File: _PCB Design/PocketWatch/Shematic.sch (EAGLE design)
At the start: 1 part

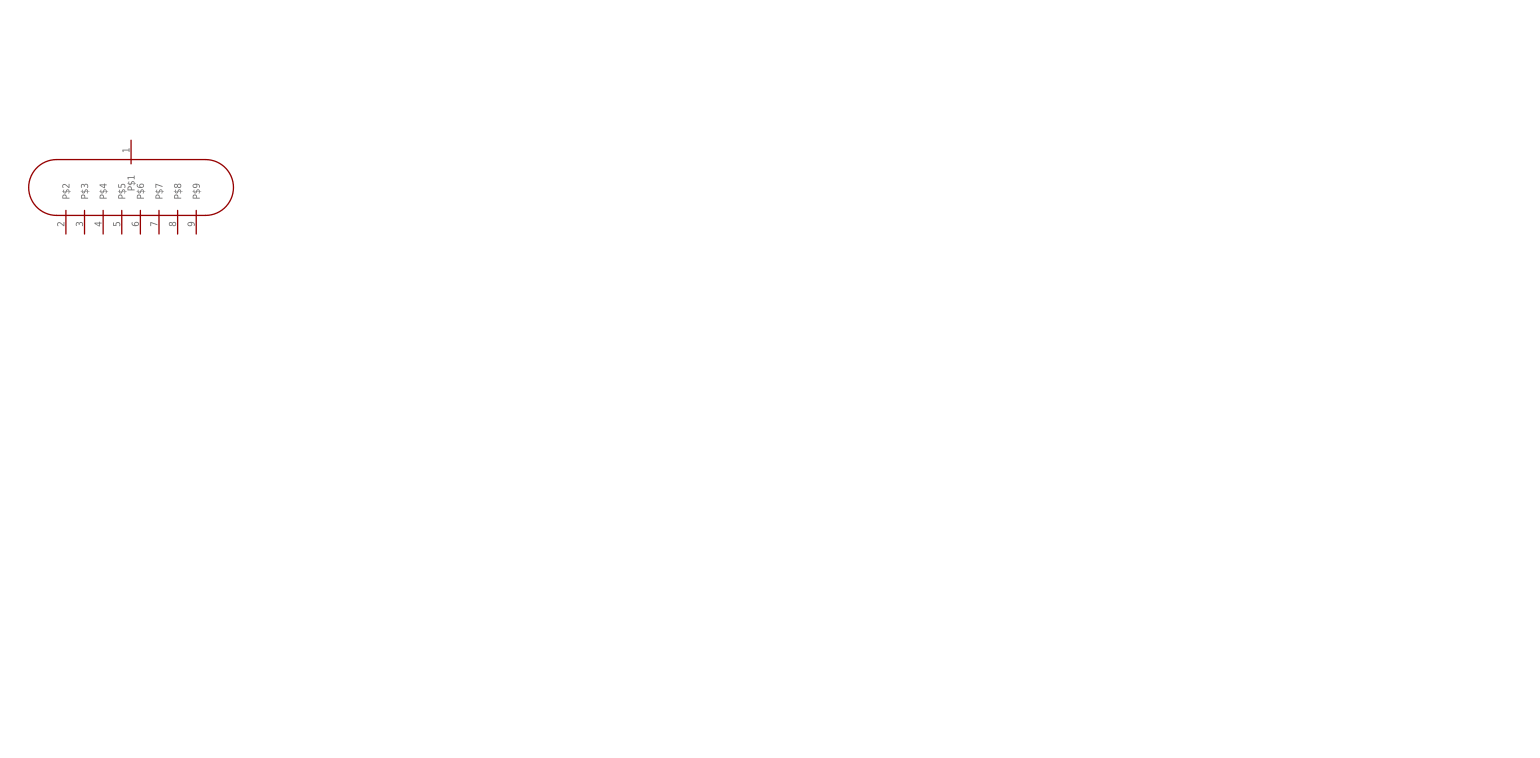
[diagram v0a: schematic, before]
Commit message: Connected IV-9 tubes to microcontroller
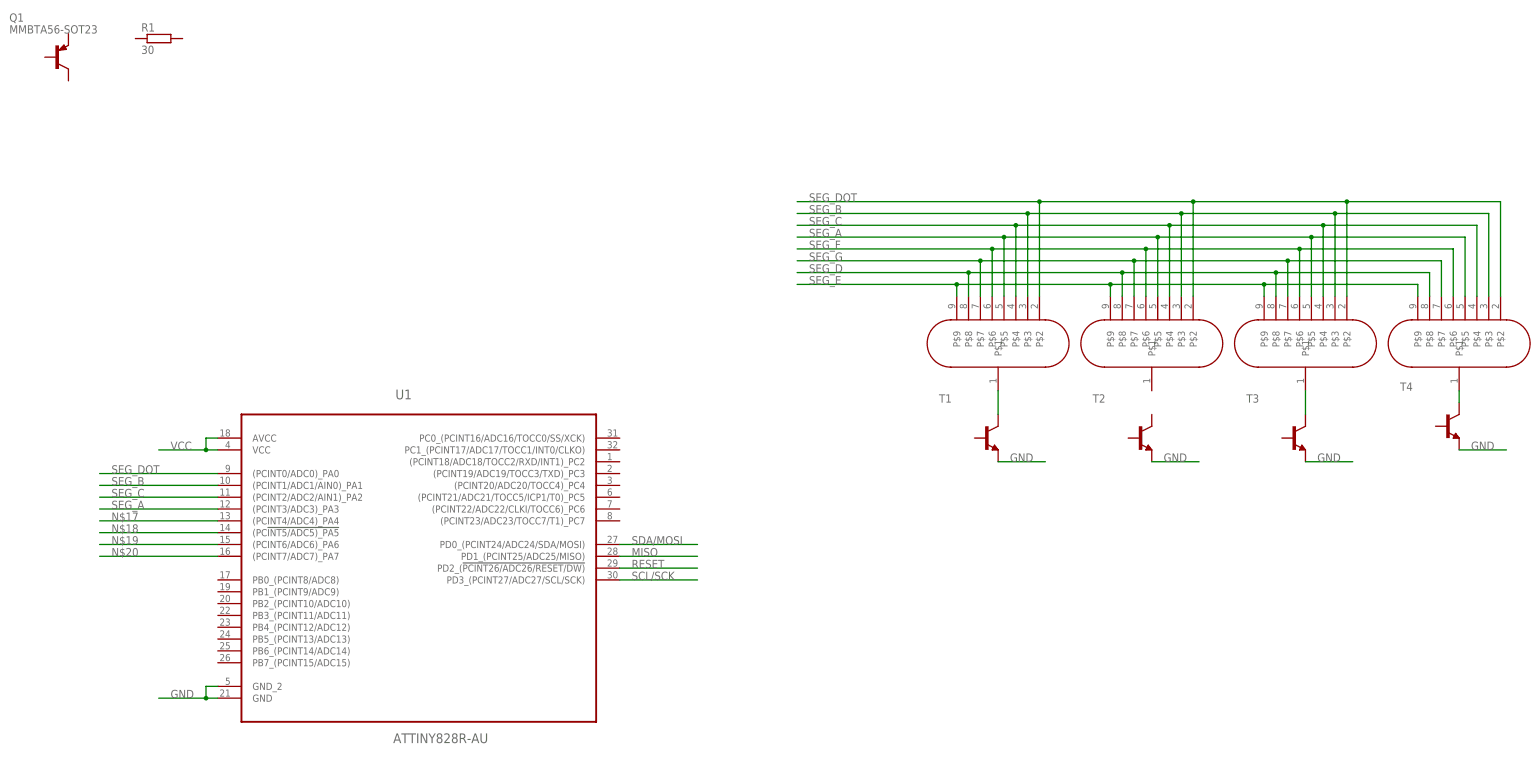
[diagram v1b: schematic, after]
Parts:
- added Q1: MMBTA56-SOT23, transistor-pnp:MMBTA56-SOT23
- added R1: 30, eagle-ltspice:RR1206
- added T1, T2, T3, T4: (no value), transistor:MMBT918LT1-NPN-SOT23-BEC
- added U$2, U$3, U$4: IV-9, Library:IV-9
- added U1: ATTINY828R-AU, Library:ATTINY828R-AU
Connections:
- new net GND: T1.E, T2.E, T3.E, T4.E, U1.GND, U1.GND_2
- new net MISO: U1.PD1_(PCINT25/ADC25/MISO)
- new net N$17: U1.(PCINT4/ADC4)_PA4
- new net N$18: U1.(PC!INT5/ADC5)_PA5
- new net N$19: U1.(PCINT6/ADC6)_PA6
- new net N$2: T3.C, U$2.P$1
- new net N$20: U1.(PCINT7/ADC7)_PA7
- new net N$3: T4.C, U$1.P$1
- new net N$5: T1.C, U$3.P$1
- new net RESET: U1.PD2_(!PCINT26/ADC26/RESET/DW)
- new net SCL/SCK: U1.PD3_(PCINT27/ADC27/SCL/SCK)
- new net SDA/MOSI: U1.PD0_(PCINT24/ADC24/SDA/MOSI)
- new net SEG_A: U$1.P$5, U$2.P$5, U$3.P$5, U$4.P$5, U1.(PCINT3/ADC3)_PA3
- new net SEG_B: U$1.P$3, U$2.P$3, U$3.P$3, U$4.P$3, U1.(PCINT1/ADC1/AIN0)_PA1
- new net SEG_C: U$1.P$4, U$2.P$4, U$3.P$4, U$4.P$4, U1.(PCINT2/ADC2/AIN1)_PA2
- new net SEG_D: U$1.P$8, U$2.P$8, U$3.P$8, U$4.P$8
- new net SEG_DOT: U$1.P$2, U$2.P$2, U$3.P$2, U$4.P$2, U1.(PCINT0/ADC0)_PA0
- new net SEG_E: U$1.P$9, U$2.P$9, U$3.P$9, U$4.P$9
- new net SEG_F: U$1.P$6, U$2.P$6, U$3.P$6, U$4.P$6
- new net SEG_G: U$1.P$7, U$2.P$7, U$3.P$7, U$4.P$7
- new net VCC: U1.AVCC, U1.VCC

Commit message: Switched design to use ATTINY88 instead of ATTINY828R to gain master I2C functionality.
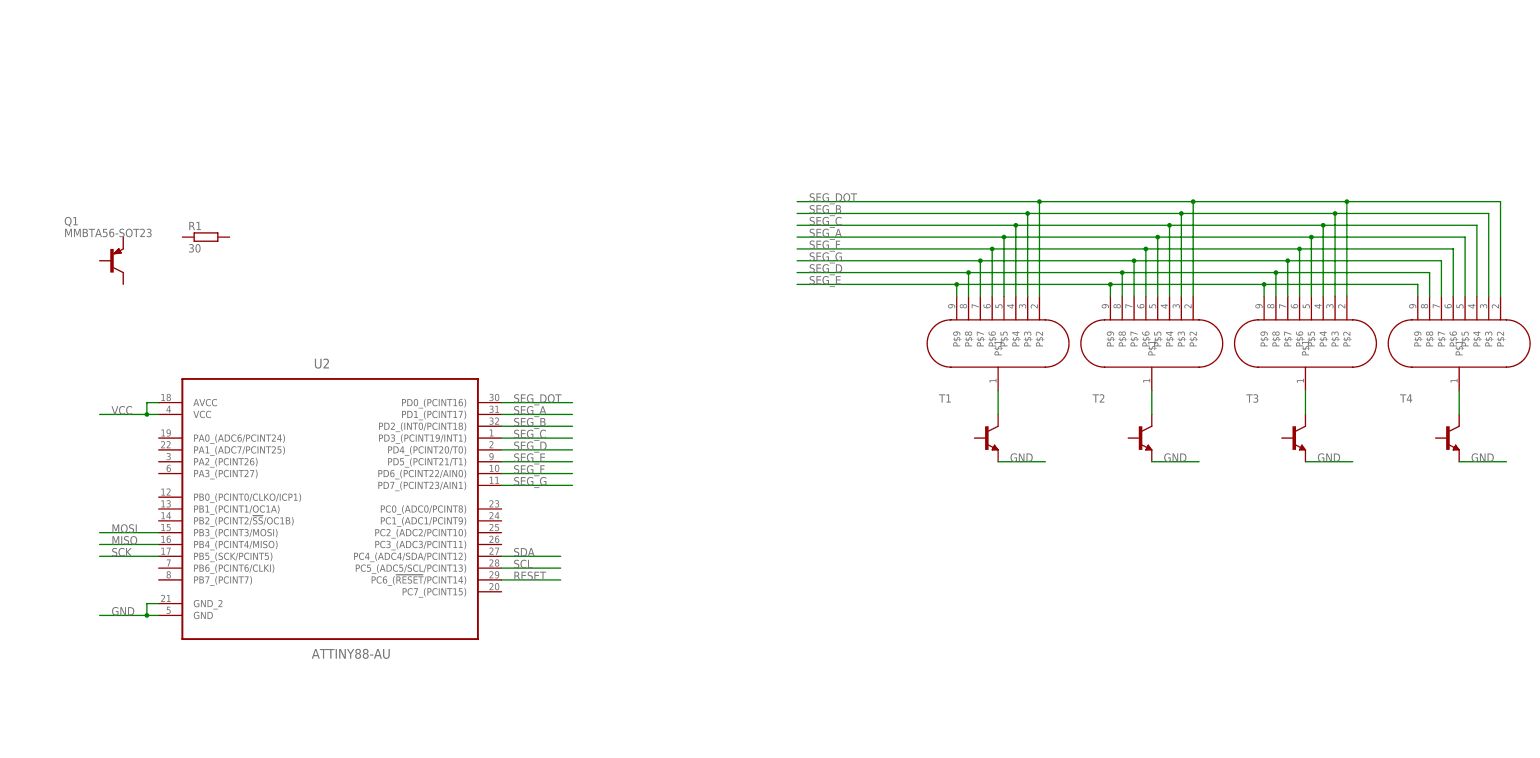
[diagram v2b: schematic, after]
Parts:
- removed U1: ATTINY828R-AU, Library:ATTINY828R-AU
- added U2: ATTINY88-AU, Library:ATTINY88-AU
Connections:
- removed net N$17: U1.(PCINT4/ADC4)_PA4
- removed net N$18: U1.(PC!INT5/ADC5)_PA5
- removed net N$19: U1.(PCINT6/ADC6)_PA6
- removed net N$20: U1.(PCINT7/ADC7)_PA7
- removed net SCL/SCK: U1.PD3_(PCINT27/ADC27/SCL/SCK)
- removed net SDA/MOSI: U1.PD0_(PCINT24/ADC24/SDA/MOSI)
- new net MOSI: U2.PB3_(PCINT3/MOSI)
- new net N$1: T2.C, U$4.P$1
- new net SCK: U2.PB5_(SCK/PCINT5)
- new net SCL: U2.PC5_(ADC5/SCL/PCINT13)
- new net SDA: U2.PC4_(ADC4/SDA/PCINT12)
- net GND: now also U2.GND, U2.GND_2; no longer U1.GND, U1.GND_2
- net MISO: now also U2.PB4_(PCINT4/MISO); no longer U1.PD1_(PCINT25/ADC25/MISO)
- net RESET: now also U2.PC6_(!RESET!/PCINT14); no longer U1.PD2_(!PCINT26/ADC26/RESET/DW)
- net SEG_A: now also U2.PD1_(PCINT17); no longer U1.(PCINT3/ADC3)_PA3
- net SEG_B: now also U2.PD2_(INT0/PCINT18); no longer U1.(PCINT1/ADC1/AIN0)_PA1
- net SEG_C: now also U2.PD3_(PCINT19/INT1); no longer U1.(PCINT2/ADC2/AIN1)_PA2
- net SEG_D: now also U2.PD4_(PCINT20/T0)
- net SEG_DOT: now also U2.PD0_(PCINT16); no longer U1.(PCINT0/ADC0)_PA0
- net SEG_E: now also U2.PD5_(PCINT21/T1)
- net SEG_F: now also U2.PD6_(PCINT22/AIN0)
- net SEG_G: now also U2.PD7_(PCINT23/AIN1)
- net VCC: now also U2.AVCC, U2.VCC; no longer U1.AVCC, U1.VCC
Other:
- moved on the sheet: Q1, R1, T4

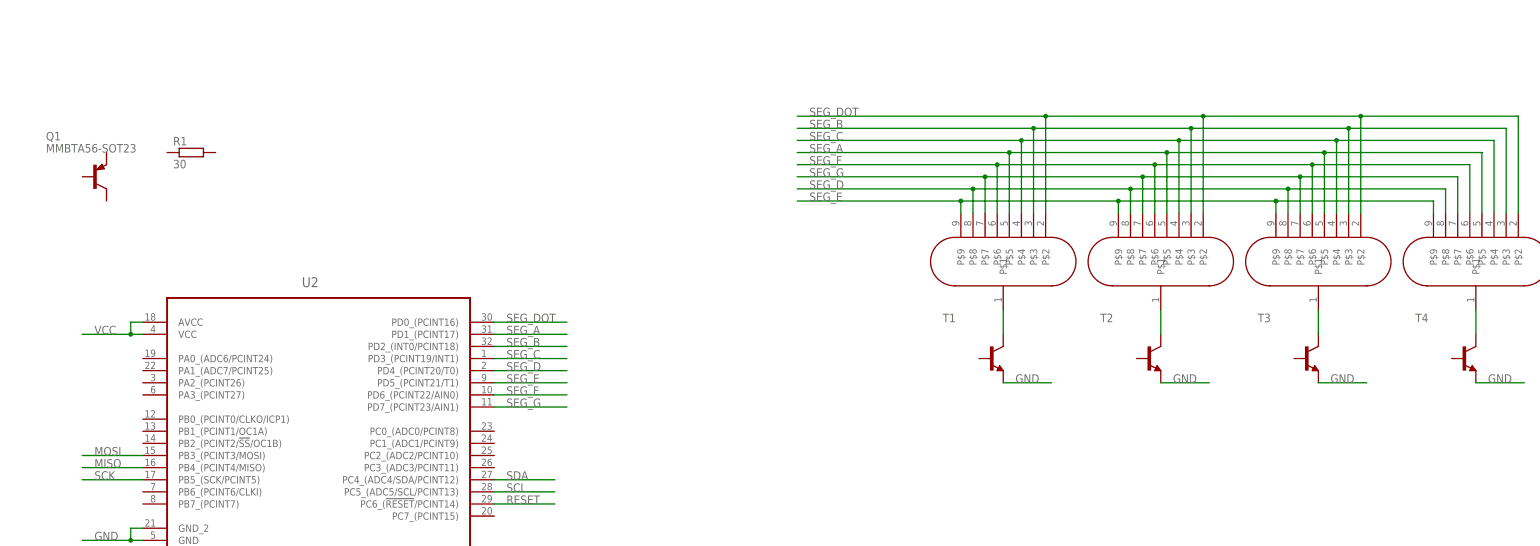
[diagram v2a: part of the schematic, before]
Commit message: Added RTC
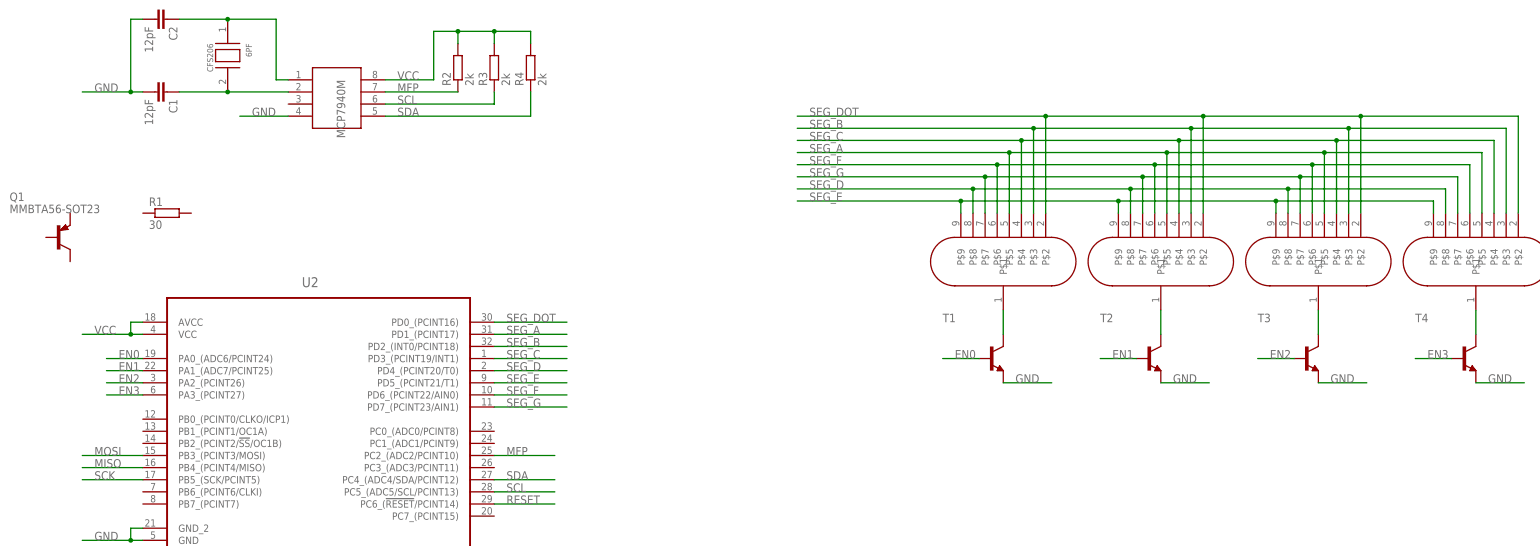
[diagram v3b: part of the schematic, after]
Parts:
- added 6PF: CFS206, Library:CFS206
- added C1, C2: 12pF, eagle-ltspice:CC1206
- added MCP7940M: SOIC-8, smd-footprints:SOIC-8
- added R2, R3, R4: 2k, eagle-ltspice:RR1206
- added U$5: FX135, Library:FX135
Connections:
- new net EN0: T1.B, U2.PA0_(ADC6/PCINT24)
- new net EN1: T2.B, U2.PA1_(ADC7/PCINT25)
- new net EN2: T3.B, U2.PA2_(PCINT26)
- new net EN3: T4.B, U2.PA3_(PCINT27)
- new net MFP: MCP7940M.P$7, R2.1, U2.PC2_(ADC2/PCINT10)
- new net N$4: 6PF.P$2, C1.1, MCP7940M.P$2
- new net N$6: 6PF.P$1, C2.1, MCP7940M.P$1
- net GND: now also C1.2, C2.2, MCP7940M.P$4
- net SCL: now also MCP7940M.P$6, R3.1
- net SDA: now also MCP7940M.P$5, R4.1
- net VCC: now also MCP7940M.P$8, R2.2, R3.2, R4.2
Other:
- moved on the sheet: Q1, R1

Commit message: Added Voltage Regulator, Designed for tubes to be on second board.
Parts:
- removed U$5: FX135, Library:FX135
- added C3: 12pF, eagle-ltspice:CC1206
- added C4, C5: 10uF, eagle-ltspice:CC1206
- added NCP1117: DPAK, smd-footprints:DPAK
- added PAD1: WIREPAD2,54/1,1, wirepad:WIREPAD2,54/1,1
- added SV1, SV2: (no value), con-lstb:MA08-1
- added SV3, SV4, SV5: (no value), con-lstb:MA04-1
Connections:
- removed net N$1: T2.C, U$4.P$1
- removed net N$2: T3.C, U$2.P$1
- removed net N$3: T4.C, U$1.P$1
- removed net N$5: T1.C, U$3.P$1
- new net SEG_A_2: SV2.4, U$1.P$5, U$2.P$5, U$3.P$5, U$4.P$5
- new net SEG_B_2: SV2.2, U$1.P$3, U$2.P$3, U$3.P$3, U$4.P$3
- new net SEG_C_2: SV2.3, U$1.P$4, U$2.P$4, U$3.P$4, U$4.P$4
- new net SEG_DOT_2: SV2.1, U$1.P$2, U$2.P$2, U$3.P$2, U$4.P$2
- new net SEG_D_2: SV2.7, U$1.P$8, U$2.P$8, U$3.P$8, U$4.P$8
- new net SEG_E_2: SV2.8, U$1.P$9, U$2.P$9, U$3.P$9, U$4.P$9
- new net SEG_F_2: SV2.5, U$1.P$6, U$2.P$6, U$3.P$6, U$4.P$6
- new net SEG_G_2: SV2.6, U$1.P$7, U$2.P$7, U$3.P$7, U$4.P$7
- new net TG0: SV5.4, T1.C
- new net TG0_2: SV3.4, U$3.P$1
- new net TG1: SV5.3, T2.C
- new net TG1_2: SV3.3, U$4.P$1
- new net TG2: SV5.2
- new net TG2_2: SV3.2, U$2.P$1
- new net TG3: SV5.1, T3.C
- new net TG3_2: SV3.1, U$1.P$1
- new net TG4: T4.C
- new net VIN: C4.1, NCP1117.P$3
- net EN0: now also SV4.4
- net EN1: now also SV4.3
- net EN2: now also SV4.2
- net EN3: now also SV4.1
- net GND: now also C4.2, C5.2, NCP1117.P$1
- net SEG_A: now also SV1.2; no longer U$1.P$5, U$2.P$5, U$3.P$5, U$4.P$5
- net SEG_B: now also SV1.3; no longer U$1.P$3, U$2.P$3, U$3.P$3, U$4.P$3
- net SEG_C: now also SV1.4; no longer U$1.P$4, U$2.P$4, U$3.P$4, U$4.P$4
- net SEG_D: now also SV1.5; no longer U$1.P$8, U$2.P$8, U$3.P$8, U$4.P$8
- net SEG_DOT: now also SV1.1; no longer U$1.P$2, U$2.P$2, U$3.P$2, U$4.P$2
- net SEG_E: now also SV1.6; no longer U$1.P$9, U$2.P$9, U$3.P$9, U$4.P$9
- net SEG_F: now also SV1.7; no longer U$1.P$6, U$2.P$6, U$3.P$6, U$4.P$6
- net SEG_G: now also SV1.8; no longer U$1.P$7, U$2.P$7, U$3.P$7, U$4.P$7
- net VCC: now also C5.1, NCP1117.P$2
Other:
- moved on the sheet: Q1, R1, T1, T2, T3, T4
